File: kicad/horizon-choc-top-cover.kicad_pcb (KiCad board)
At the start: 2 copper layers, 36 x 34 mm, 6 parts

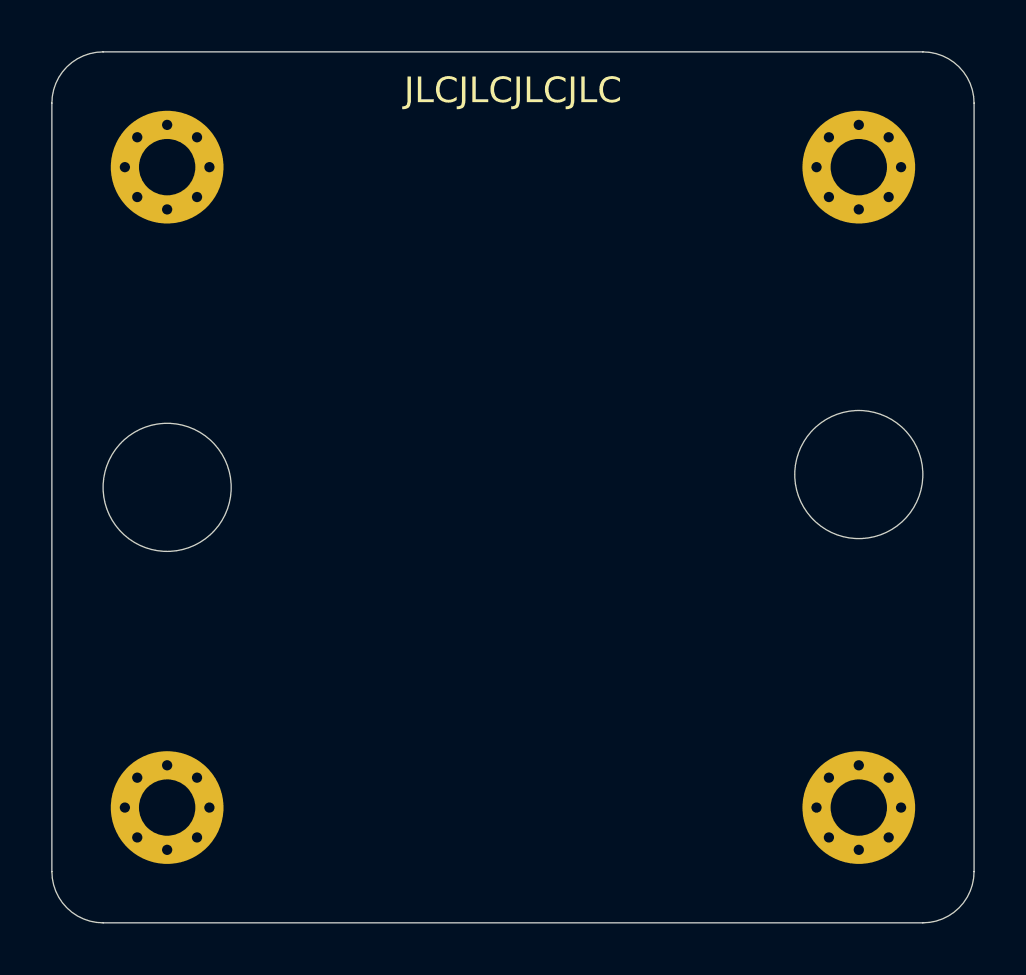
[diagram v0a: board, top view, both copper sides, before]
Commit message: Use 50-key layout
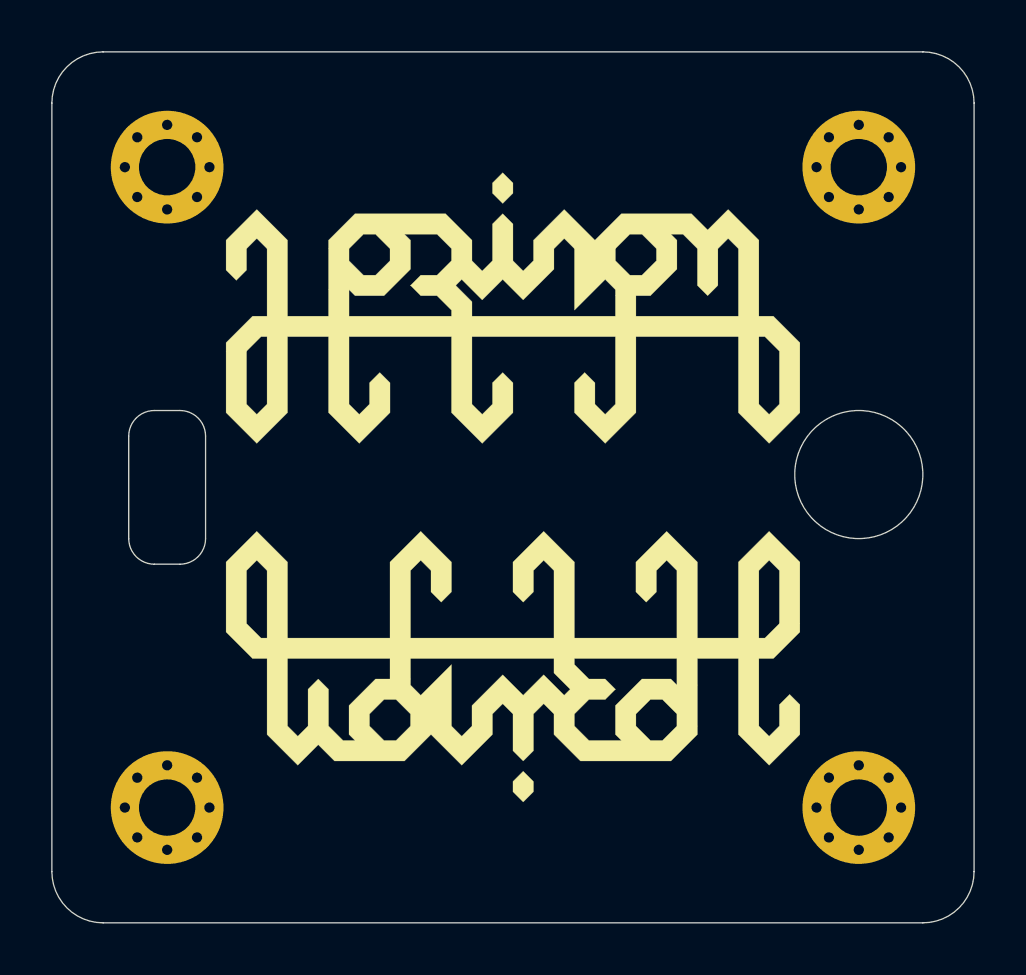
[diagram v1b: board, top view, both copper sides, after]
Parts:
- G*** (x2): moved to F.Cu
- turned G*** to 0 degrees
- turned G*** to 180 degrees
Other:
- outline, holes or cut-outs redrawn

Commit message: Layout MX PCB
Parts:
- removed the G*** at (202.0, 119.0)
- moved G*** 7.16 mm to (205.0, 111.5)
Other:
- outline, holes or cut-outs redrawn
- board text added: "OFF"
- board text added: "ON"
- board text added: "RESET"

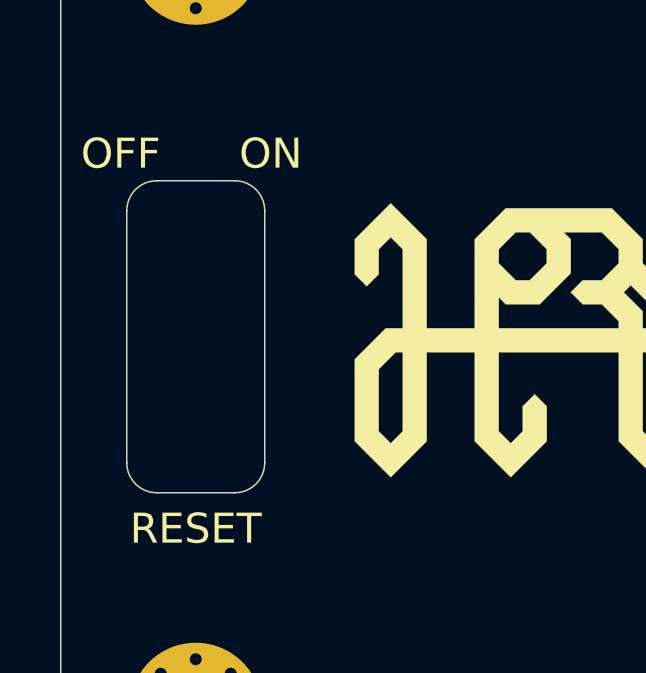
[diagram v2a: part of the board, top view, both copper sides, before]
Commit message: Mark bottom plate cutout on footprint adhesive layer. Begin writing bottom plate generation script
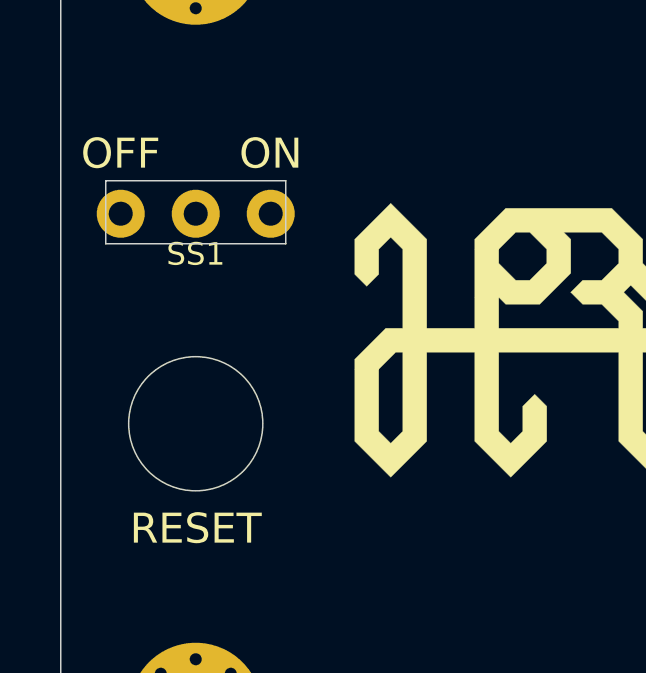
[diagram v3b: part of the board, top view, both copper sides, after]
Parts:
- added SS1: POWER, horizon-footprints:SS12D00, F.Cu at (188.5, 108.0)
- renumbered H12 to ?, H11 to ?, H10 to ?, H9 to ?
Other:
- outline, holes or cut-outs redrawn
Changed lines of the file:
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@@
   (general
     (thickness 1.6)
-    (drawings 20)
+    (drawings 17)
     (tracks 0)
     (zones 0)
-    (modules 5)
+    (modules 6)
     (nets 5)
   )
@@
     (diff_pair_width 0.2)
     (diff_pair_gap 0.3)
+  )
+  (module horizon-footprints:SS12D00 (layer F.Cu)
+    (at 188.5 108)
+    (descr "SS12D00 SPDT Slide Switch")
+    (tags "SPDT, slide switch")
+    (fp_text reference SS1 (at 0 1.35) (layer F.SilkS)
+      (effects (font (size 0.75 0.75) (thickness 0.15)))
+    )
+    (fp_text value POWER (at 0 -1.35) (layer F.Fab)
+      (effects (font (size 0.75 0.75) (thickness 0.15)))
+    )
+    (fp_line (start -4.25 -1.75) (end 4.25 -1.75) (layer F.CrtYd) (width 0.1))
+    (fp_line (start -4.25 1.75) (end 4.25 1.75) (layer F.CrtYd) (width 0.1))
+    (fp_line (start -4.25 -1.75) (end -4.25 1.75) (layer F.CrtYd) (width 0.1))
+    (fp_line (start 4.25 -1.75) (end 4.25 1.75) (layer F.CrtYd) (width 0.1))
+    (fp_line (start -1.75 -0.8) (end 1.75 -0.8) (layer Dwgs.User) (width 0.15))
+    (fp_line (start -1.75 0.8) (end 1.75 0.8) (layer Dwgs.User) (width 0.15))
+    (fp_line (start -1.75 -0.8) (end -1.75 0.8) (layer Dwgs.User) (width 0.15))
+    (fp_line (start 1.75 -0.8) (end 1.75 0.8) (layer Dwgs.User) (width 0.15))
+    (pad 1 thru_hole circle (at -2.5 0) (size 1.6 1.6) (drill 0.8) (layers *.Cu *.Mask))
+    (pad 2 thru_hole circle (at 0 0) (size 1.6 1.6) (drill 0.8) (layers *.Cu *.Mask))
+    (pad 3 thru_hole circle (at 2.5 0) (size 1.6 1.6) (drill 0.8) (layers *.Cu *.Mask))
   )
   (module horizon-footprints:Logo_Horizon (layer F.Cu)
@@
     (tags "mounting hole 2.2mm m2")
     (attr virtual)
-    (fp_text reference H12 (at 0 -3.25) (layer F.SilkS) hide
+    (fp_text reference "" (at 0 -3.25) (layer F.SilkS) hide
       (effects (font (size 1 1) (thickness 0.15)))
     )
@@
     (tags "mounting hole 2.2mm m2")
     (attr virtual)
-    (fp_text reference H11 (at 0 -3.25) (layer F.SilkS) hide
+    (fp_text reference "" (at 0 -3.25) (layer F.SilkS) hide
       (effects (font (size 1 1) (thickness 0.15)))
     )
@@
     (tags "mounting hole 2.2mm m2")
     (attr virtual)
-    (fp_text reference H10 (at 0 -3.25) (layer F.SilkS) hide
+    (fp_text reference "" (at 0 -3.25) (layer F.SilkS) hide
       (effects (font (size 1 1) (thickness 0.15)))
     )
@@
     (tags "mounting hole 2.2mm m2")
     (attr virtual)
-    (fp_text reference H9 (at 0 -3.25) (layer F.SilkS) hide
+    (fp_text reference "" (at 0 -3.25) (layer F.SilkS) hide
       (effects (font (size 1 1) (thickness 0.15)))
     )
@@
       (net 1 "Net-(H9-Pad1)"))
   )
-  (gr_arc (start 189.8 116.3) (end 189.8 117.3) (angle -90) (layer Edge.Cuts) (width 0.05))
-  (gr_arc (start 187.2 116.3) (end 186.2 116.3) (angle -90) (layer Edge.Cuts) (width 0.05))
-  (gr_arc (start 189.8 107.9) (end 190.8 107.9) (angle -90) (layer Edge.Cuts) (width 0.05))
-  (gr_arc (start 187.2 107.9) (end 187.2 106.9) (angle -90) (layer Edge.Cuts) (width 0.05))
+  (gr_line (start 191.5 106.9) (end 191.5 109) (layer Edge.Cuts) (width 0.05))
+  (gr_line (start 185.5 106.9) (end 185.5 109) (layer Edge.Cuts) (width 0.05))
+  (gr_line (start 191.5 109) (end 185.5 109) (layer Edge.Cuts) (width 0.05))
+  (gr_circle (center 188.5 115) (end 190.5 116) (layer Edge.Cuts) (width 0.05))
   (gr_text ON (at 191 106) (layer F.SilkS)
     (effects (font (size 1 1) (thickness 0.15)))
@@
     (effects (font (size 1 1) (thickness 0.15)))
   )
-  (gr_line (start 189.8 106.9) (end 187.2 106.9) (layer Edge.Cuts) (width 0.05))
-  (gr_line (start 190.8 116.3) (end 190.8 107.9) (layer Edge.Cuts) (width 0.05))
-  (gr_line (start 187.2 117.3) (end 189.8 117.3) (layer Edge.Cuts) (width 0.05))
-  (gr_line (start 186.2 107.9) (end 186.2 116.3) (layer Edge.Cuts) (width 0.05))
+  (gr_line (start 191.5 106.9) (end 185.5 106.9) (layer Edge.Cuts) (width 0.05))
   (gr_arc (start 186 127) (end 184 127) (angle -90) (layer Edge.Cuts) (width 0.05))
   (gr_arc (start 218 127) (end 218 129) (angle -90) (layer Edge.Cuts) (width 0.05))
